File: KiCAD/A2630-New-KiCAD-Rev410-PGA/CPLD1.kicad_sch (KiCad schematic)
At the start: 16 parts, among them CN600 CPLD0, CN601 CPLD1, CN602 CPLD2, U600 XC9572XL-10VQ64, U601 XC95144XL-10TQ144, U602 XC95144XL-10TQ144

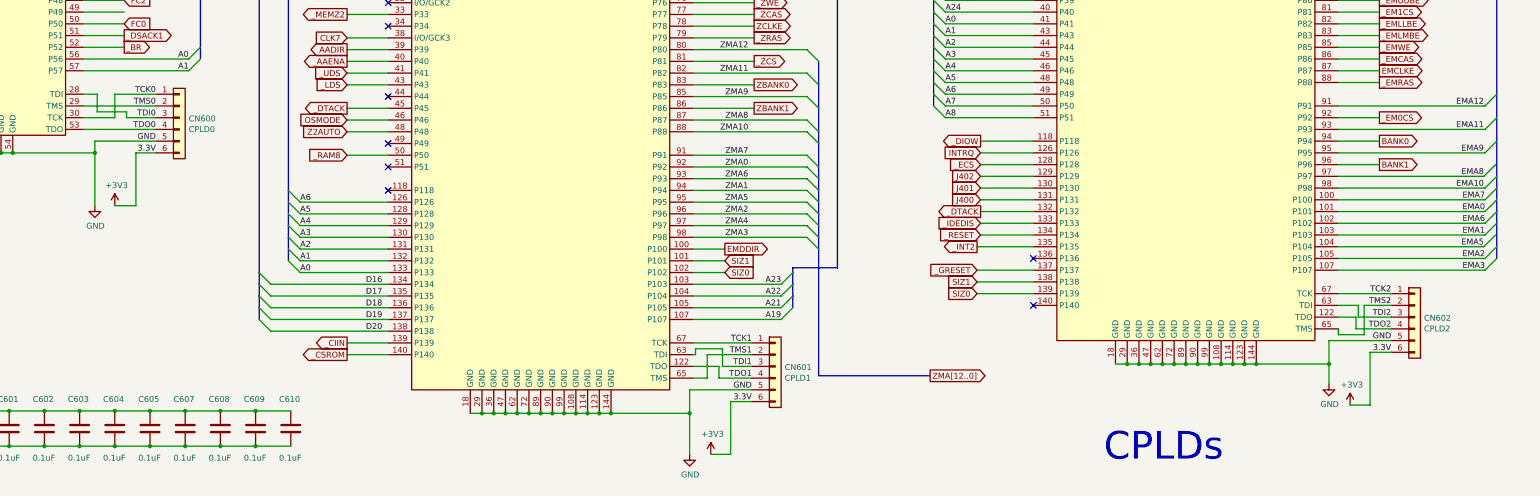
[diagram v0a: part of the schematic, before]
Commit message: Better for SMD assembly now. DRC still not done.
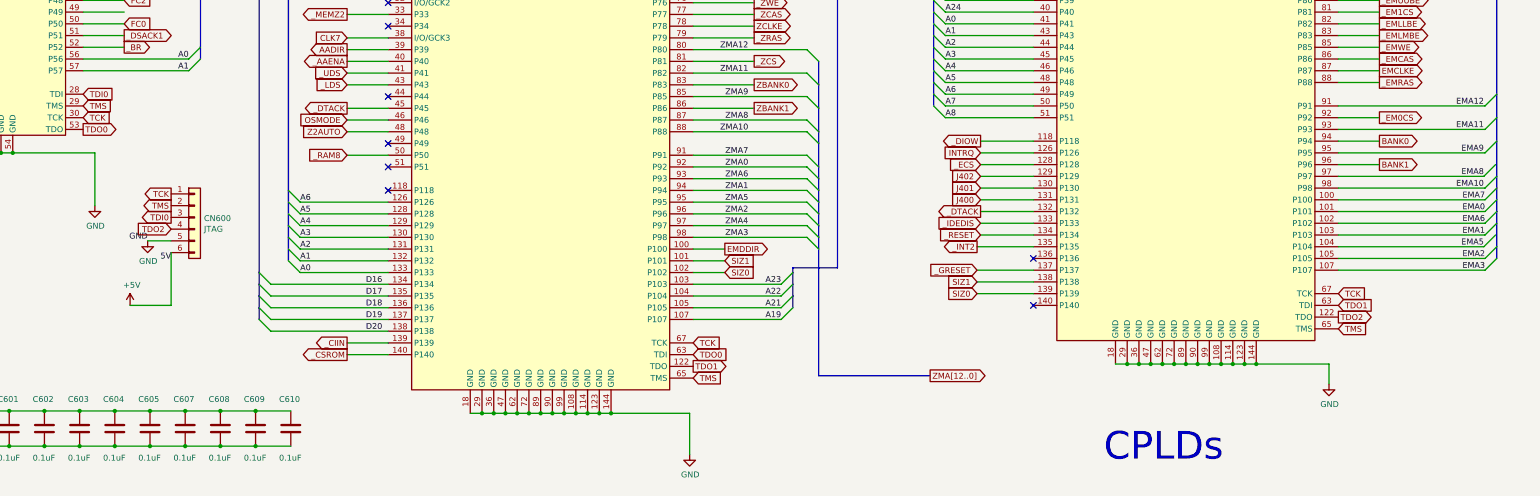
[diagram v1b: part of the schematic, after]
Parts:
- removed CN601: CPLD1, Connector_PinHeader_2.54mm:PinHeader_1x06_P2.54mm_Vertical, symbol Connector_Generic:Conn_01x06
- removed CN602: CPLD2, Connector_PinHeader_2.54mm:PinHeader_1x06_P2.54mm_Vertical, symbol Connector_Generic:Conn_01x06
- C600, C601, C602, C603, C604, C605, C607, C608, C609, C610: LCSC (none) -> C49678
- CN600: value CPLD0 -> JTAG
- U600: LCSC (none) -> C90569
- U601, U602: LCSC (none) -> C1521137
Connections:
- net TCK1 is gone; now on net TCK: U601.67 (TCK)
- net TCK2 is gone; now on net TCK: U602.67 (TCK)
- net TDI1 is gone; now on net TDO0: U601.63 (TDI)
- net TDI2 is gone; now on net TDO1: U602.63 (TDI)
- net TMS1 is gone; now on net TMS: U601.65 (TMS)
- net TMS2 is gone; now on net TMS: U602.65 (TMS)
- net +3V3: no longer CN600.6 (Pin_6)
- net TDO0: no longer CN600.4 (Pin_4)
- net TDO2: now also CN600.4 (Pin_4)
- net TCK0 renamed TCK
- net TMS0 renamed TMS
- new net +5V: CN600.6 (Pin_6)
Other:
- moved on the sheet: CN600
